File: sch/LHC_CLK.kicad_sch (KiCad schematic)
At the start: 1 part, among them U1 Si5395

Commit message: sfp+ sheet
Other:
- company: (none) -> Karlsruhe Institute of Technology (KIT)
- title: (none) -> ATCA Simple Loopback HUB
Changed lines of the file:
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@@
 (kicad_sch (version 20230121) (generator eeschema)
   (paper "A4")
+  (title_block
+    (title "ATCA Simple Loopback HUB")
+    (date "2023-09-12")
+    (rev "1.0")
+    (company "Karlsruhe Institute of Technology (KIT)")
+    (comment 1 "Institute for Data Processing and Electronics (IPE)")
+    (comment 2 "Luis Ardila")
+    (comment 3 "IPE-380-06")
+    (comment 4 "Licensed under CERN-OHL-P-2.0")
+  )
   (bus_entry (at 208.28 69.85) (size 2.54 -2.54)
     (stroke (width 0) (type default))

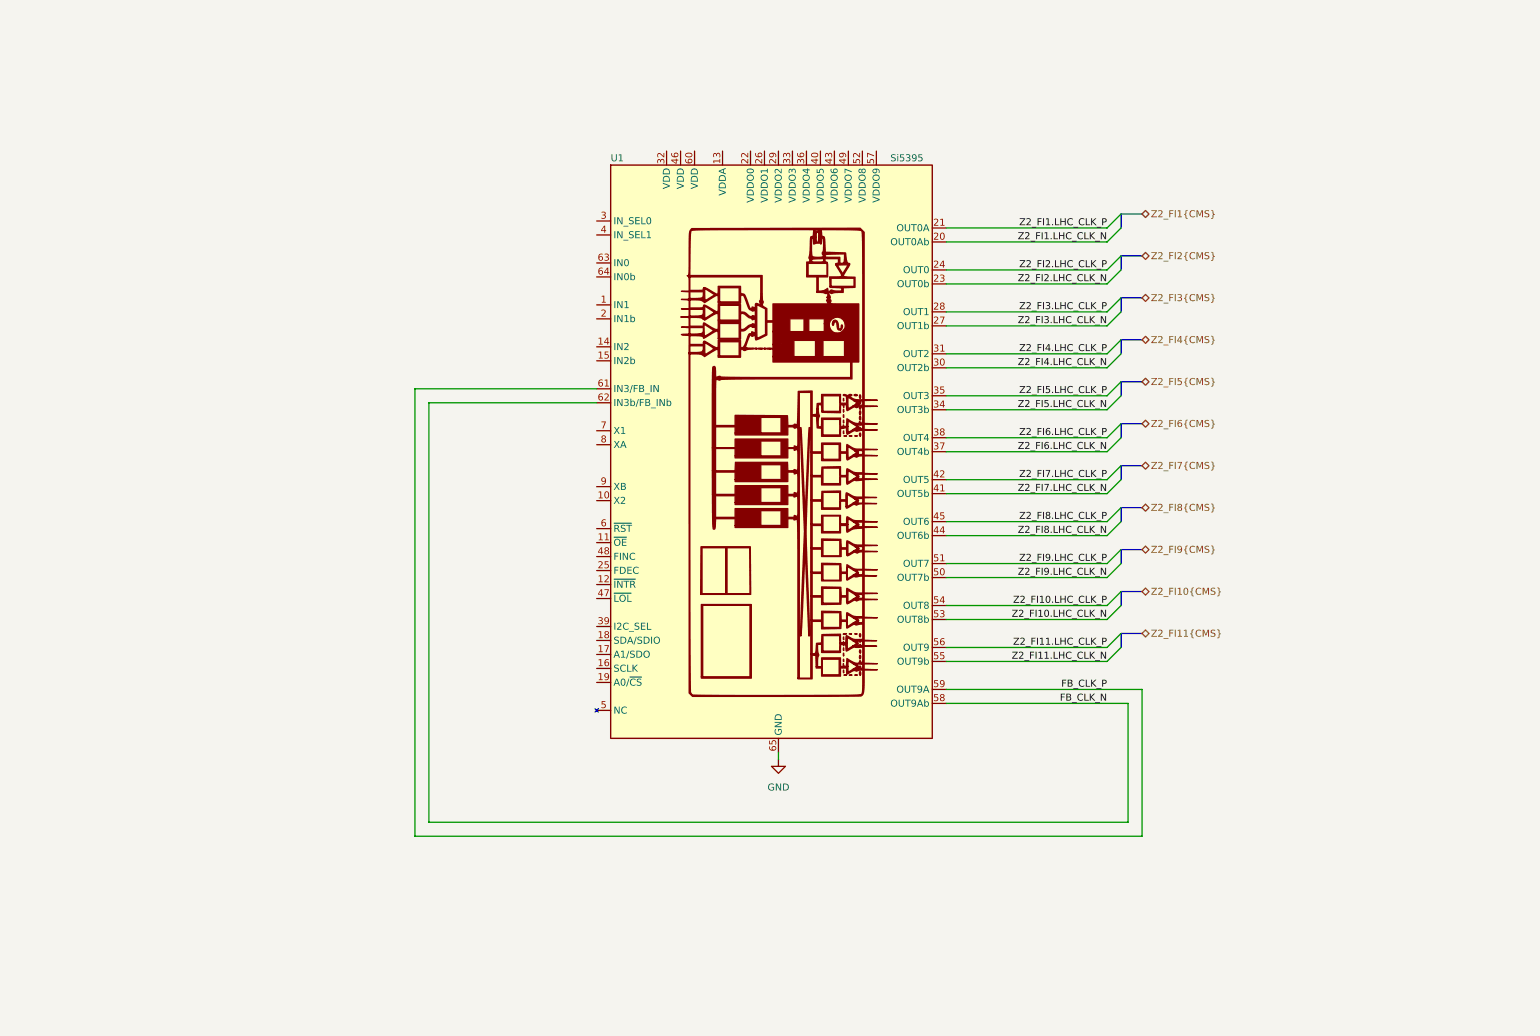
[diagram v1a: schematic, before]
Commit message: work on sc pll and pll sheet
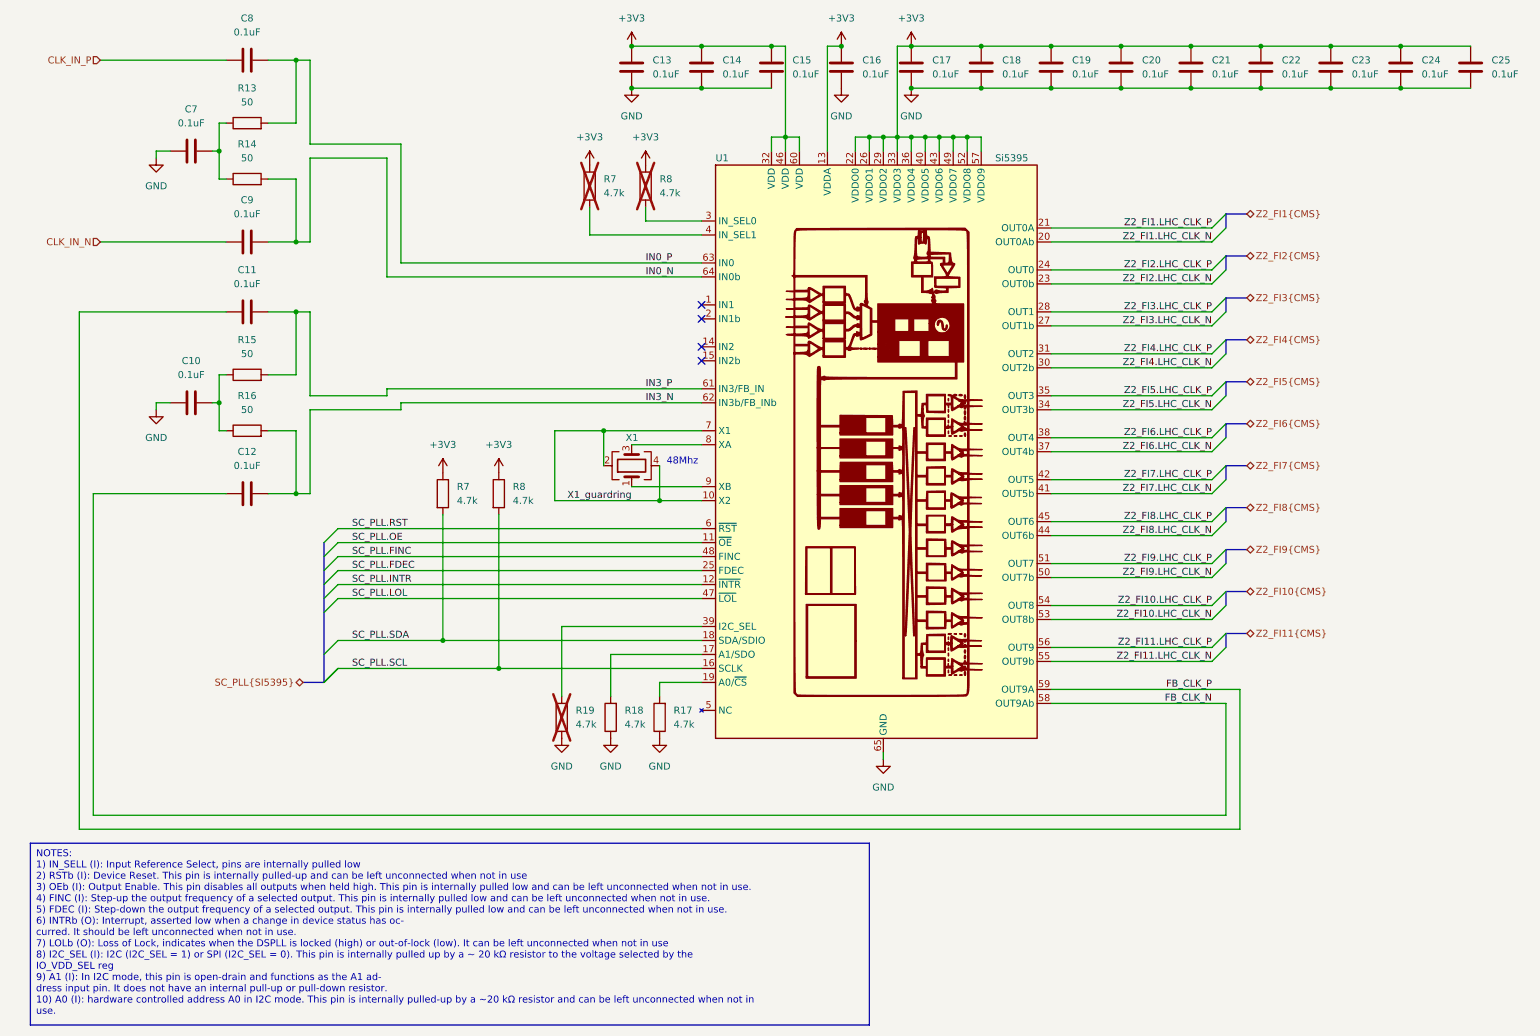
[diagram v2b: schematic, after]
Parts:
- added C10, C11, C12, C13, C14, C15, C16, C17, C18, C19, C20, C21, C22, C23, C24, C25, C7, C8, C9: 0.1uF, Capacitor_SMD:C_0402_1005Metric, symbol Device:C
- added R13, R14, R15, R16: 50, Resistor_SMD:R_0402_1005Metric, symbol Device:R
- added R17, R18, R19, R7 (x2), R8 (x2): 4.7k, Resistor_SMD:R_0402_1005Metric, symbol Device:R
- added X1: CX3225SB, Crystal:Crystal_SMD_3225-4Pin_3.2x2.5mm, symbol Device:Crystal_GND24
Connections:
- net FB_CLK_N: now also C12.1; no longer U1.62 (IN3b/FB_INb)
- net FB_CLK_P: now also C11.1; no longer U1.61 (IN3/FB_IN)
- net GND: now also C10.1, C13.1, C14.1, C15.1, C16.1, C17.1, C18.1, C19.1, C20.1, C21.1, C22.1, C23.1, C24.1, C25.1, C7.1, R17.1, R18.1, R19.1
- net X1_guardring: now reaches U1.10 (X2)
- net X1_guardring: now also U1.7 (X1), X1.2, X1.4
- net SC_PLL.OE: now reaches U1.11 (~{OE})
- net SC_PLL.INTR: now reaches U1.12 (~{INTR})
- net +3V3: now reaches U1.13 (VDDA)
- net +3V3: now also U1.22 (VDDO0), U1.26 (VDDO1), U1.29 (VDDO2), U1.32 (VDD), U1.33 (VDDO3), U1.36 (VDDO4), U1.40 (VDDO5), U1.43 (VDDO6), U1.46 (VDD), U1.49 (VDDO7), U1.52 (VDDO8), U1.57 (VDDO9), U1.60 (VDD), C13.2, C14.2, C15.2, C16.2, C17.2, C18.2, C19.2, C20.2, C21.2, C22.2, C23.2, C24.2, C25.2, R7.1, R7.1, R8.1, R8.1
- net SC_PLL.SCL: now reaches U1.16 (SCLK)
- net SC_PLL.SCL: now also R8.2
- net at U1.17 (A1/SDO): now also R18.2
- net SC_PLL.SDA: now reaches U1.18 (SDA/SDIO)
- net SC_PLL.SDA: now also R7.2
- net at U1.19 (A0/~{CS}): now also R17.2
- net SC_PLL.FDEC: now reaches U1.25 (FDEC)
- net at U1.3 (IN_SEL0): now also R8.2
- net at U1.39 (I2C_SEL): now also R19.2
- net at U1.4 (IN_SEL1): now also R7.2
- net SC_PLL.LOL: now reaches U1.47 (~{LOL})
- net SC_PLL.FINC: now reaches U1.48 (FINC)
- net SC_PLL.RST: now reaches U1.6 (~{RST})
- net IN0_P: now reaches U1.63 (IN0)
- net IN0_P: now also C8.2, R13.2
- net IN0_N: now reaches U1.64 (IN0b)
- net IN0_N: now also C9.2, R14.2
- net at U1.8 (XA): now also X1.3
- net at U1.9 (XB): now also X1.1
- new net: C10.2, R15.1, R16.1
- new net: C7.2, R13.1, R14.1
- new net CLK_IN_N: C9.1
- new net CLK_IN_P: C8.1
- new net IN3_N: C12.2, R16.2, U1.62 (IN3b/FB_INb)
- new net IN3_P: C11.2, R15.2, U1.61 (IN3/FB_IN)
- no-connect marks 0 -> 4
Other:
- note added: "48Mhz"
- moved on the sheet: U1

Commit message: sch work
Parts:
- removed R7, R8: 4.7k, Resistor_SMD:R_0402_1005Metric, symbol Device:R
- added FB1: FerriteBead, Inductor_SMD:L_0603_1608Metric, symbol Device:FerriteBead
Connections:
- net +3V3: now also FB1.1; no longer C13.2, C14.2, C15.2, C16.2, U1.13 (VDDA), U1.32 (VDD), U1.46 (VDD), U1.60 (VDD)
- new net +1V8: C13.2, C14.2, C15.2, U1.32 (VDD), U1.46 (VDD), U1.60 (VDD)
- new net +VDDA: C16.2, FB1.2, U1.13 (VDDA)
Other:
- note added: "I2C Address = 8'b1101_000X, 8'hD0, 7'h68"
- moved on the sheet: C13, C14, C15

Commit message: before sch review
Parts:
- R19, R7, R8: now left out of the parts list
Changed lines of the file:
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@@
   )
   (symbol (lib_id "Device:R") (at 109.22 140.97 180) (unit 1)
-    (in_bom yes) (on_board yes) (dnp yes) (fields_autoplaced)
+    (in_bom no) (on_board yes) (dnp yes) (fields_autoplaced)
     (property "Reference" "R19" (at 111.76 139.7 0)
       (effects (font (size 1.27 1.27)) (justify right))
@@
   )
   (symbol (lib_id "Device:R") (at 114.3 44.45 0) (unit 1)
-    (in_bom yes) (on_board yes) (dnp yes) (fields_autoplaced)
+    (in_bom no) (on_board yes) (dnp yes) (fields_autoplaced)
     (property "Reference" "R7" (at 116.84 43.18 0)
       (effects (font (size 1.27 1.27)) (justify left))
@@
   )
   (symbol (lib_id "Device:R") (at 124.46 44.45 0) (unit 1)
-    (in_bom yes) (on_board yes) (dnp yes) (fields_autoplaced)
+    (in_bom no) (on_board yes) (dnp yes) (fields_autoplaced)
     (property "Reference" "R8" (at 127 43.18 0)
       (effects (font (size 1.27 1.27)) (justify left))

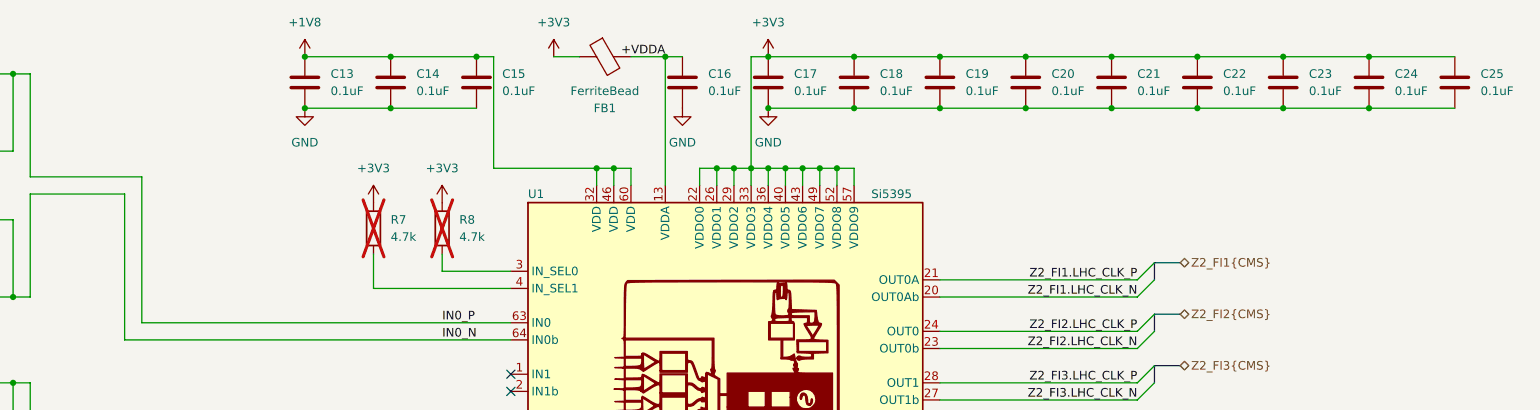
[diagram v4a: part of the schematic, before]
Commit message: started changes from review
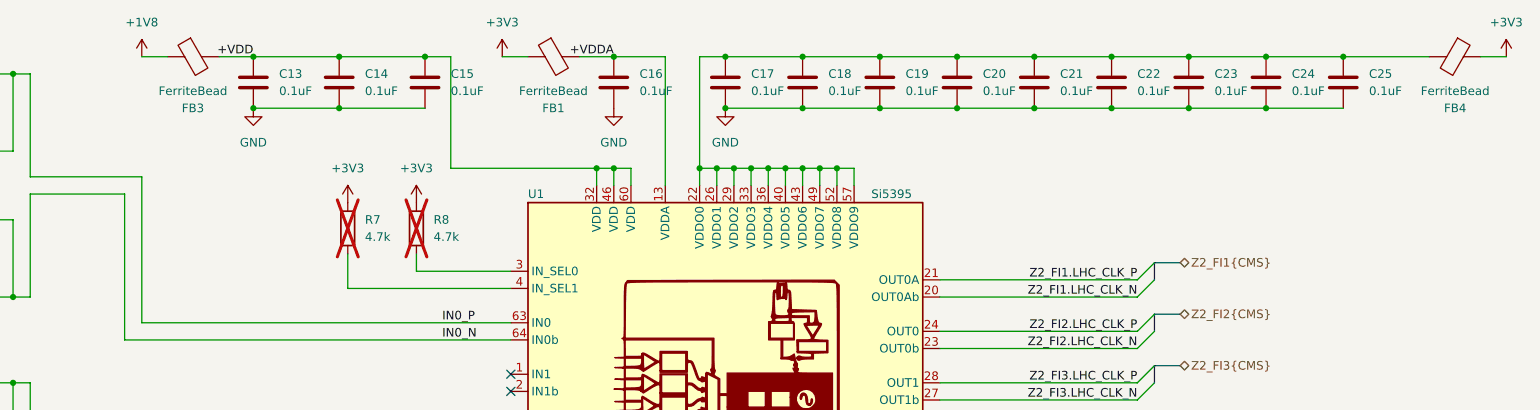
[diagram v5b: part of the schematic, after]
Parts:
- added FB3, FB4: FerriteBead, Inductor_SMD:L_0603_1608Metric, symbol Device:FerriteBead
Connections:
- net +1V8: now also FB3.1; no longer C13.2, C14.2, C15.2, U1.32 (VDD), U1.46 (VDD), U1.60 (VDD)
- net +3V3: now also FB4.1; no longer C17.2, C18.2, C19.2, C20.2, C21.2, C22.2, C23.2, C24.2, C25.2, U1.22 (VDDO0), U1.26 (VDDO1), U1.29 (VDDO2), U1.33 (VDDO3), U1.36 (VDDO4), U1.40 (VDDO5), U1.43 (VDDO6), U1.49 (VDDO7), U1.52 (VDDO8), U1.57 (VDDO9)
- new net: C17.2, C18.2, C19.2, C20.2, C21.2, C22.2, C23.2, C24.2, C25.2, FB4.2, U1.22 (VDDO0), U1.26 (VDDO1), U1.29 (VDDO2), U1.33 (VDDO3), U1.36 (VDDO4), U1.40 (VDDO5), U1.43 (VDDO6), U1.49 (VDDO7), U1.52 (VDDO8), U1.57 (VDDO9)
- new net +VDD: C13.2, C14.2, C15.2, FB3.2, U1.32 (VDD), U1.46 (VDD), U1.60 (VDD)
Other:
- moved on the sheet: C13, C14, C15, C16, C17, C18, C19, C20, C21, C22, C23, C24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

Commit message: starting doing stackup calculations
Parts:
- C13, C14, C15, C16: value 0.1uF -> 1uF
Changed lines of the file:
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@@
       (effects (font (size 1.27 1.27)) (justify right))
     )
-    (property "Value" "0.1uF" (at 153.67 24.13 0)
+    (property "Value" "1uF" (at 153.67 24.13 0)
       (effects (font (size 1.27 1.27)) (justify right))
     )
@@
       (effects (font (size 1.27 1.27)) (justify right))
     )
-    (property "Value" "0.1uF" (at 113.03 24.13 0)
+    (property "Value" "1uF" (at 113.03 24.13 0)
       (effects (font (size 1.27 1.27)) (justify right))
     )
@@
       (effects (font (size 1.27 1.27)) (justify right))
     )
-    (property "Value" "0.1uF" (at 100.33 24.13 0)
+    (property "Value" "1uF" (at 100.33 24.13 0)
       (effects (font (size 1.27 1.27)) (justify right))
     )
@@
       (effects (font (size 1.27 1.27)) (justify right))
     )
-    (property "Value" "0.1uF" (at 125.73 24.13 0)
-      (effects (font (size 1.27 1.27)) (justify right))
-    )
+    (property "Value" "1uF" (at 125.73 24.13 0)
+      (effects (font (size 1.27 1.27)) (justify right))
+    )

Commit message: update to v8
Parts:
- renumbered R7 to R22, R8 to R23

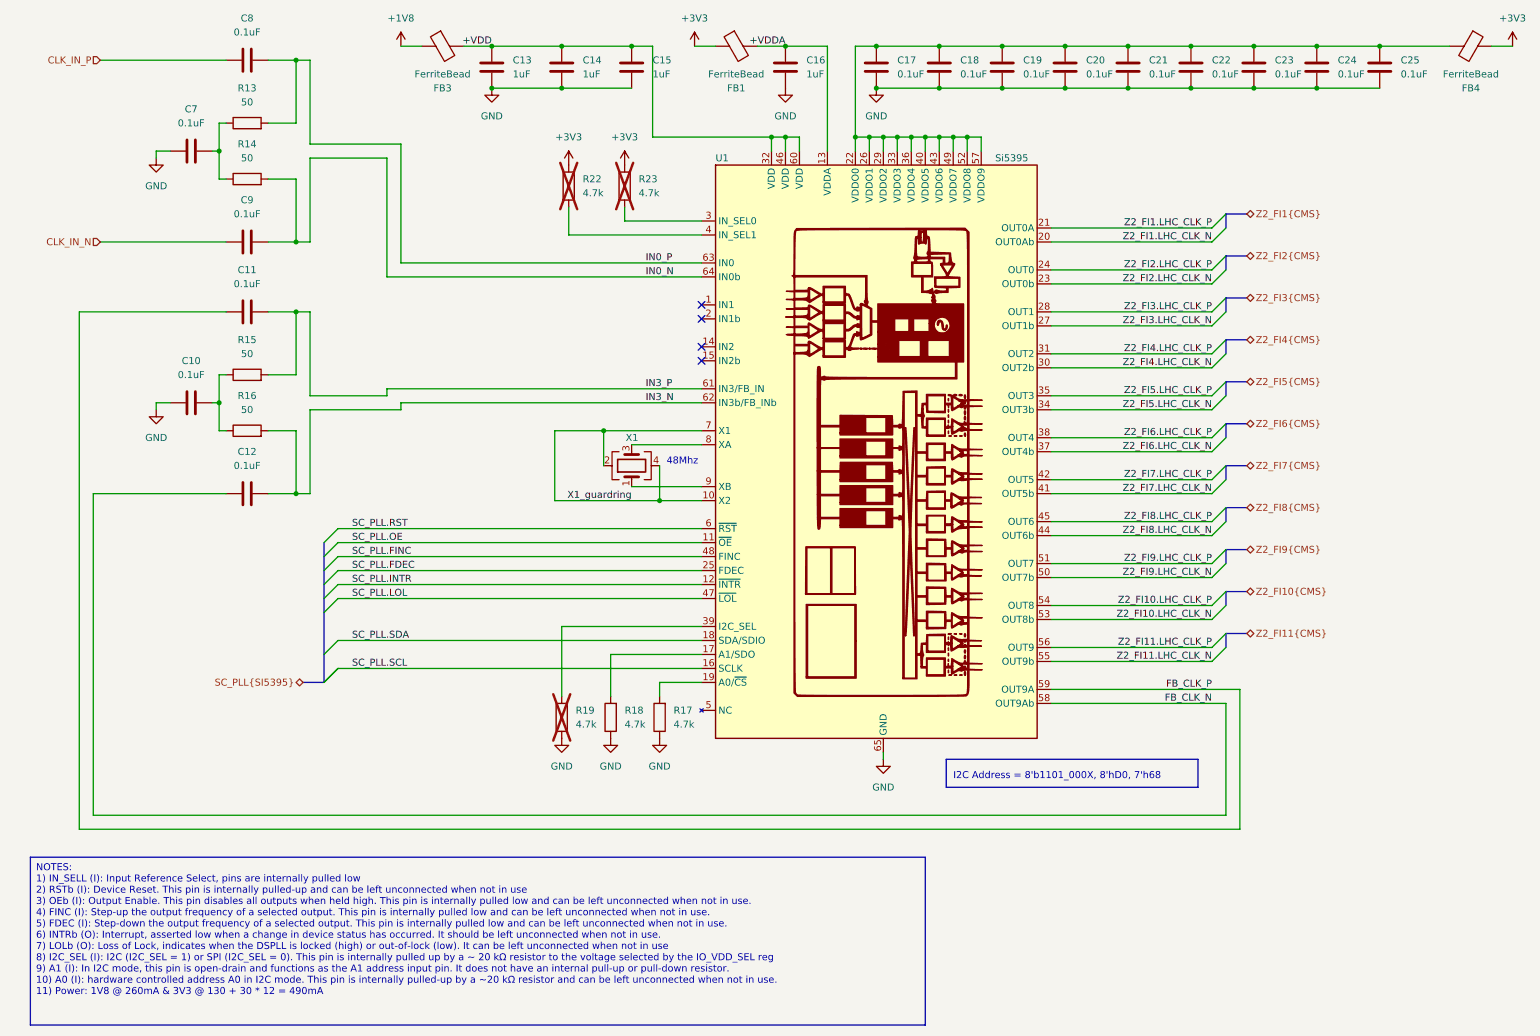
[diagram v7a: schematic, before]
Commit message: added loop between plls and monitoring sma at the second stage pll
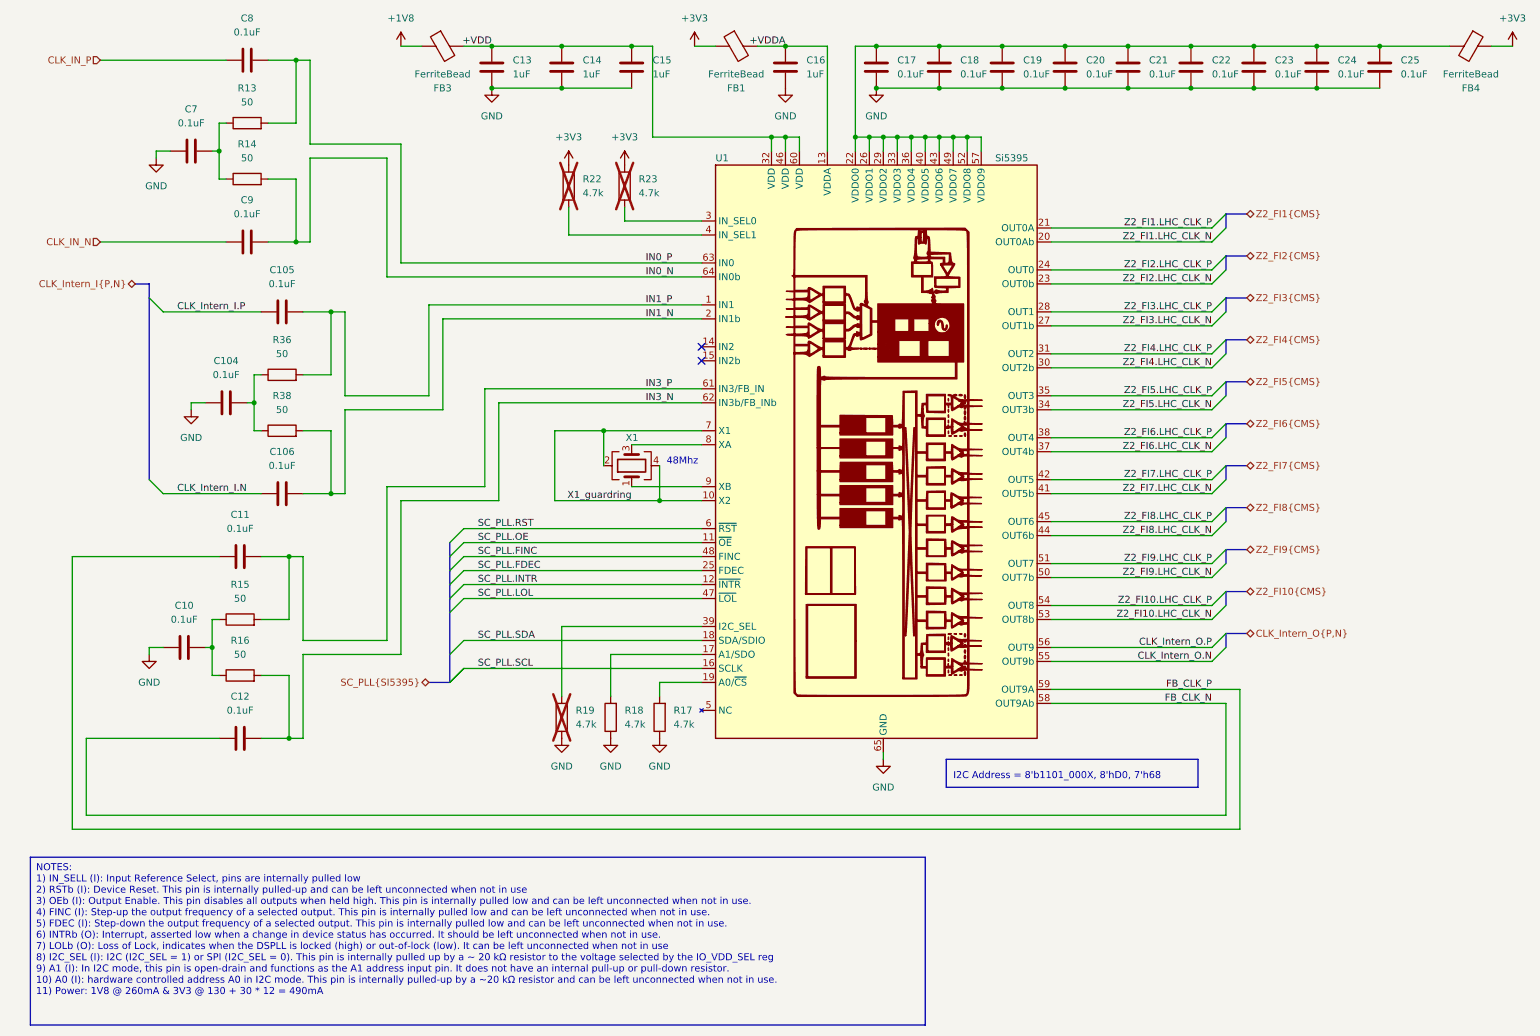
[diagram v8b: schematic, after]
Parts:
- added C104, C105, C106: 0.1uF, Capacitor_SMD:C_0402_1005Metric, symbol Device:C
- added R36, R38: 50, Resistor_SMD:R_0402_1005Metric, symbol Device:R
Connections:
- net GND: now also C104.1
- net IN1_P: now reaches U1.1 (IN1)
- net IN1_P: now also C105.2, R36.2
- net IN1_N: now reaches U1.2 (IN1b)
- net IN1_N: now also C106.2, R38.2
- net Z2_FI11.LHC_CLK_N renamed CLK_Intern_O.N
- net Z2_FI11.LHC_CLK_P renamed CLK_Intern_O.P
- new net: C104.2, R36.1, R38.1
- new net CLK_Intern_I.N: C106.1
- new net CLK_Intern_I.P: C105.1
- no-connect marks 4 -> 2
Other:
- moved on the sheet: C10, C11, C12, R15, R16
